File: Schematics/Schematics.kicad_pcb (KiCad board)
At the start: 2 copper layers, 85 x 90 mm, 19 parts, among them U1 TP4056, U2 BH1750, U3 BME688, U4 BU30TD3WG, U5 NRF52840-DONGLE, U6 LIS3DH

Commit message: Generated gerber and bom files
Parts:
- moved BT1 0.35 mm to (167.5, 105.0)
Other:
- outline, holes or cut-outs redrawn

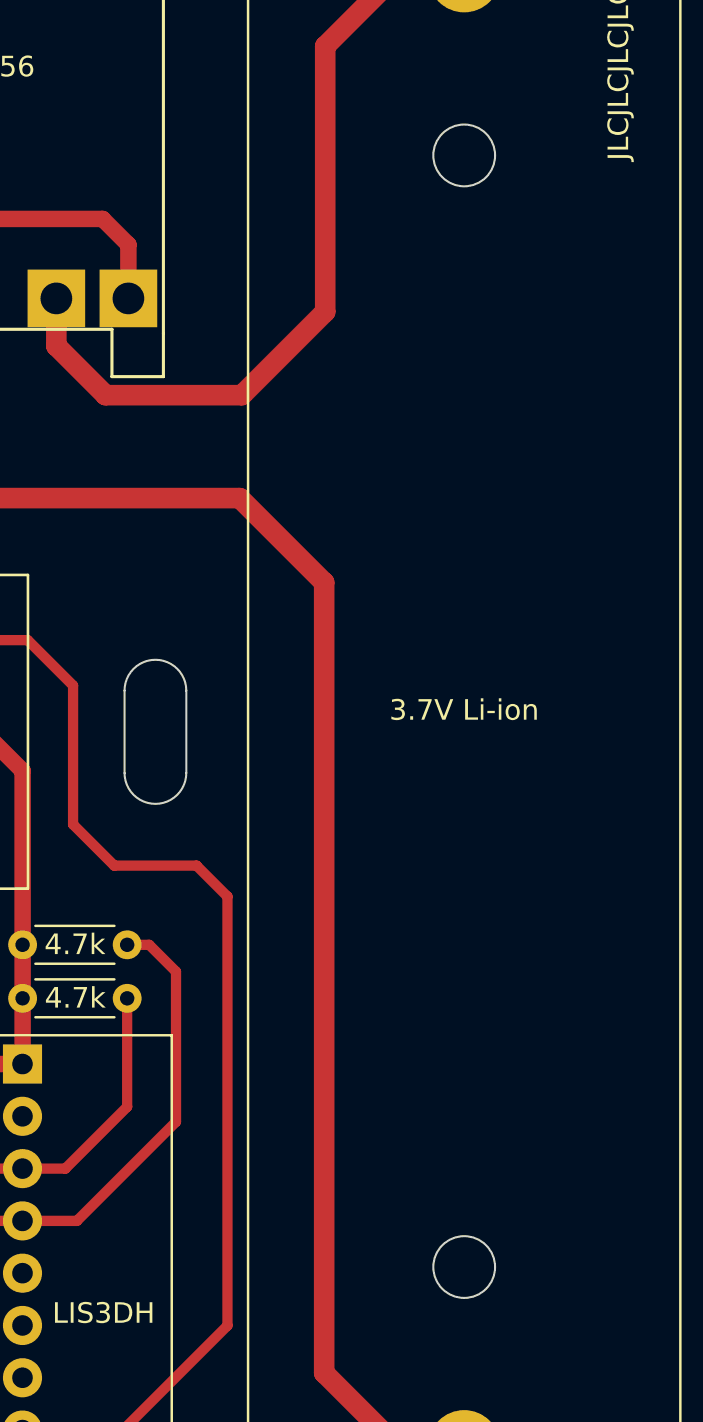
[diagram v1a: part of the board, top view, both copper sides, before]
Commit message: Edited the pcb board of the vodesht_vyzel and did some small changes on the pcb of the main module
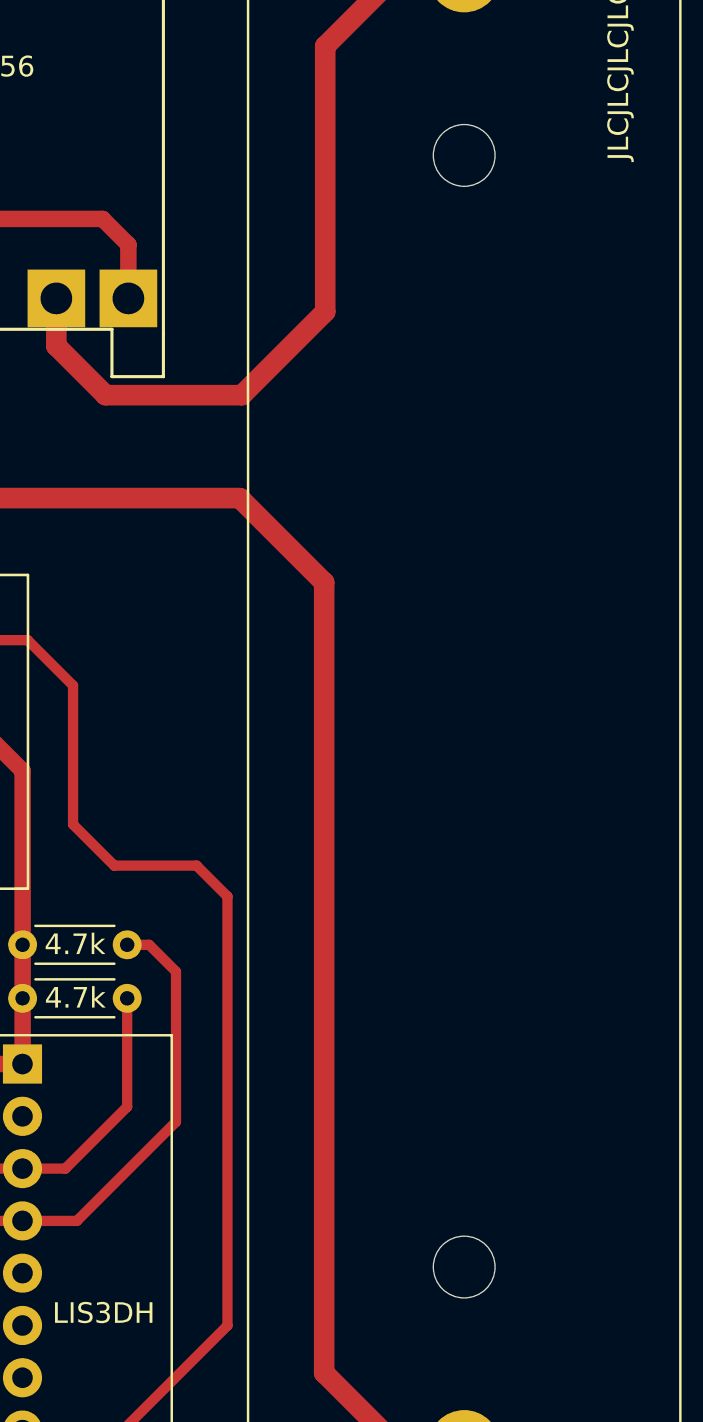
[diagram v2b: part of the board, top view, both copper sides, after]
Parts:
- added H5: MountingHole, custom:Slot, F.Cu at (152.5, 106.0)
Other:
- outline, holes or cut-outs redrawn
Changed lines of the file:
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@@
       (disableapertmacros false)
       (usegerberextensions true)
-      (usegerberattributes true)
-      (usegerberadvancedattributes true)
+      (usegerberattributes false)
+      (usegerberadvancedattributes false)
       (creategerberjobfile false)
       (svguseinch false)
@@
       (drillshape 0)
       (scaleselection 1)
-      (outputdirectory "gerber_and_drill_files/x2 experiment/")
+      (outputdirectory "gerber_and_drill_files/")
     )
   )
@@
     (pad "" np_thru_hole circle locked (at 0 0) (size 2.5 2.5) (drill 2.5) (layers F&B.Cu *.Mask))
   )
+  (footprint "custom:Slot" (layer "F.Cu")
+    (at 152.5 106)
+    (property "Sheetfile" "Schematics.kicad_sch")
+    (property "Sheetname" "")
+    (attr through_hole)
+    (fp_text reference "H5" (at 0.5 -5 unlocked) (layer "F.SilkS") hide
+      (effects (font (size 1 1) (thickness 0.15)))
+    )
+    (fp_text value "MountingHole" (at 0 4.5 unlocked) (layer "F.Fab") hide
+      (effects (font (size 1 1) (thickness 0.15)))
+    )
+    (fp_text user "${REFERENCE}" (at 0 5 unlocked) (layer "F.Fab") hide
+      (effects (font (size 1 1) (thickness 0.15)))
+    )
+    (pad "" np_thru_hole oval (at 0 0) (size 3 7) (drill oval 3 7) (layers F&B.Cu *.Mask))
+  )
   (footprint "Capacitor_THT:C_Disc_D5.1mm_W3.2mm_P5.00mm" (layer "F.Cu")
     (at 124.988 88.446)
@@
       (effects (font (size 1 1) (thickness 0.15)))
     )
-    (fp_text value "3.7V Li-ion" (at -0.05 0 unlocked) (layer "F.SilkS")
+    (fp_text value "3.7V Li-ion" (at -0.05 0 unlocked) (layer "F.Fab")
       (effects (font (size 1 1) (thickness 0.15)))
     )
@@
       (effects (font (size 3 3) (thickness 0.15)))
     )
-    (fp_text user "${REFERENCE}" (at -35.9 11.6 -90 unlocked) (layer "F.Fab") hide
+    (fp_text user "${REFERENCE}" (at -35.9 11.6 -90 unlocked) (layer "F.Fab")
       (effects (font (size 1 1) (thickness 0.15)))
     )
     (fp_line (start -37.75 10.5) (end -37.75 -10.5) (layer "F.SilkS") (width 0.12))
+    (fp_line (start -37.75 -10.5) (end 37.75 -10.5) (layer "F.SilkS") (width 0.12))
     (fp_line (start 37.75 10.5) (end 37.75 -10.5) (layer "F.SilkS") (width 0.12))
     (fp_line (start -37.75 10.5) (end 37.75 10.5) (layer "F.SilkS") (width 0.12))
-    (fp_line (start -37.75 -10.5) (end 37.75 -10.5) (layer "F.SilkS") (width 0.12))
+    (fp_line (start -37.75 10.5) (end -37.75 -10.5) (layer "F.Fab") (width 0.12))
     (fp_line (start -37.75 10.5) (end 37.75 10.5) (layer "F.Fab") (width 0.12))
-    (fp_line (start -37.75 10.5) (end -37.75 -10.5) (layer "F.Fab") (width 0.12))
     (fp_line (start 37.75 10.5) (end 37.75 -10.5) (layer "F.Fab") (width 0.12))
     (fp_line (start -37.75 -10.5) (end 37.75 -10.5) (layer "F.Fab") (width 0.12))
+    (fp_circle (center -27 0) (end -25.5 0) (layer "F.Fab") (width 0.2) (fill none))
     (fp_circle (center 27 0) (end 28.5 0) (layer "F.Fab") (width 0.2) (fill none))
-    (fp_circle (center -27 0) (end -25.5 0) (layer "F.Fab") (width 0.2) (fill none))
+    (pad "" np_thru_hole circle (at -27 0 270) (size 3 3) (drill 3) (layers F&B.Cu *.Mask))
+    (pad "" np_thru_hole circle (at 27 0 270) (size 3 3) (drill 3) (layers F&B.Cu *.Mask))
     (pad "1" thru_hole oval (at -35.7 0 270) (size 3.5 3.5) (drill 1.5) (layers *.Cu *.Mask)
       (net 32 "Net-(BT1-Pad1)") (pinfunction "+") (pintype "passive"))
@@
     )
   )
-  (gr_circle (center 167.5 132) (end 169 132) (layer "Edge.Cuts") (width 0.1) (fill none))
   (gr_arc (start 100 64) (mid 101.171573 61.171573) (end 104 60) (layer "Edge.Cuts") (width 0.1))
   (gr_arc (start 181 60) (mid 183.828427 61.171573) (end 185 64) (layer "Edge.Cuts") (width 0.1))
   (gr_arc (start 102 95) (mid 100.585786 94.414214) (end 100 93) (layer "Edge.Cuts") (width 0.1))
-  (gr_line (start 151 104) (end 151 108) (layer "Edge.Cuts") (width 0.1))
-  (gr_circle (center 167.5 78) (end 169 78) (layer "Edge.Cuts") (width 0.1) (fill none))
-  (gr_line (start 154 104) (end 154 108) (layer "Edge.Cuts") (width 0.1))
   (gr_line (start 185 64) (end 185 146) (layer "Edge.Cuts") (width 0.1))
   (gr_arc (start 109 95) (mid 110.414214 95.585786) (end 111 97) (layer "Edge.Cuts") (width 0.1))
   (gr_arc (start 111 115) (mid 110.414214 116.414214) (end 109 117) (layer "Edge.Cuts") (width 0.1))
   (gr_line (start 111 97) (end 111 115) (layer "Edge.Cuts") (width 0.1))
-  (gr_arc (start 151 104) (mid 152.5 102.5) (end 154 104) (layer "Edge.Cuts") (width 0.1))
   (gr_line (start 100 146) (end 100 119) (layer "Edge.Cuts") (width 0.1))
   (gr_line (start 102 117) (end 109 117) (layer "Edge.Cuts") (width 0.1))
@@
   (gr_line (start 104 60) (end 181 60) (layer "Edge.Cuts") (width 0.1))
   (gr_arc (start 100 119) (mid 100.585786 117.585786) (end 102 117) (layer "Edge.Cuts") (width 0.1))
-  (gr_arc (start 154 108) (mid 152.5 109.5) (end 151 108) (layer "Edge.Cuts") (width 0.1))
   (gr_line (start 181 150) (end 104 150) (layer "Edge.Cuts") (width 0.1))
   (gr_arc (start 104 150) (mid 101.171573 148.828427) (end 100 146) (layer "Edge.Cuts") (width 0.1))

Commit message: Final commit
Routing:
- removed copper zone on B.Cu, net GNDD
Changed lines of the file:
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@@
   (segment (start 156.598 94.646) (end 160.698 98.746) (width 1) (layer "F.Cu") (net 33))
   (segment (start 143.598 94.646) (end 156.598 94.646) (width 1) (layer "F.Cu") (net 33))
-  (zone (net 2) (net_name "GNDD") (layer "B.Cu") (hatch edge 0.508)
-    (connect_pads (clearance 0.3))
-    (min_thickness 0.2) (filled_areas_thickness no)
-    (fill yes (thermal_gap 0.5) (thermal_bridge_width 0.5))
-    (polygon
-      (pts
-        (xy 185 150)
-        (xy 100 150)
-        (xy 100 60)
-        (xy 185 60)
-      )
-    )
-  )
 )
